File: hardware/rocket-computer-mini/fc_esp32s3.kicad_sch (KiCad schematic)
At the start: 35 parts, among them SW2 R-667995, U32 ESP32-S3RH2, U33 GD25Q128ESIG, Y3 ABS07-32.768KHZ-T, Y4 ECS-400-10-37B2-CKY-TR

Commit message: hardware: BOM re-use pass, DTC123J land fix, and pyro one-shot RC rework
Re-use pass across both rocket computers. The 17 new passives per board drawn
for the pack-fire/supercap rework carried no MPN field at all and would have
exported as blank BOM lines; assigning already-stocked parts rather than new
ones collapsed 15 would-be-new lines to zero.

Pyro arm one-shot (both boards):
- R131 added in parallel with R121 (2x 1M = 500k), C133/C138 moved to the
  stocked 22uF 0805, deleting the 10uF 0805 line.
- Not just BOM tidiness: SN74LVC1G17 Ii is +/-5uA max (SCES351Y Tbl 5-1). On
  the high-impedance timer node that offsets the asymptote to Vgate - Ii*R, so
  a single 1M settles near 1.0V, under VT+ max 1.92V, and a worst-case
  conforming part would NEVER trip the crowbar - the arm gate would stay up
  indefinitely. Max permissible R at the 2.83V supervisor floor is ~590k;
  500k clears it with ~19% headroom. Do not collapse R131 back into one 1M.
- R130 22k -> stocked 10k. With C133 now 22uF the reset stays at 0.22s, so the
  two edits cancel and the >=0.5s inter-arm spacing rule is unchanged.
- Ceiling ~3.4s nominal, 1.7s fast corner. The pyro sheet note now carries the
  leakage constraint so it cannot be "simplified" away later.

DTC123J land (affects Q3-Q6 on both boards, not only the rework):
- Widened to ROHM's own recommended pattern (Land Pattern Reference,
  Transistor, Rev.001 p.1/6): pair 0.6x0.7 on 1.0mm pitch, lone pad 0.7x0.7,
  rows 1.3 c-c. The inherited land was an imperial 14x30 mil pattern, 30-50%
  narrow across the lead with almost no side fillet on the widest terminal.
- Renamed DTC123JEBTL -> TRANS_SOT-416_EMT3-EMT3F_ROHM. ROHM publishes ONE
  land for both the gull-wing EMT3 and the flat-lead EMT3F, so naming it after
  either part number was misleading.
- rocket-computer-mini Q12 -> DTC123JETL, matching its Q3-Q6. MPN field only.

NOTE: the wider pads collide with existing routing on rocket-computer - two
genuine pad-to-via shorts (Q3 GND v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
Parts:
- D10: MPN XL-1005UGC -> NCD0402R1; Mfr Xinglight -> NationStar
- D11: MPN XL-1005UGC -> APHHS1005QBC/D; Mfr Xinglight -> Kingbright
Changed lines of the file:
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@@
 			)
 		)
-		(property "MPN" "XL-1005UGC"
+		(property "MPN" "NCD0402R1"
 			(at 254 104.14 0)
 			(hide yes)
@@
 			)
 		)
-		(property "Mfr" "Xinglight"
+		(property "Mfr" "NationStar"
 			(at 254 104.14 0)
 			(hide yes)
@@
 			)
 		)
-		(property "MPN" "XL-1005UGC"
+		(property "MPN" "APHHS1005QBC/D"
 			(at 268.605 104.14 0)
 			(hide yes)
@@
 			)
 		)
-		(property "Mfr" "Xinglight"
+		(property "Mfr" "Kingbright"
 			(at 268.605 104.14 0)
 			(hide yes)

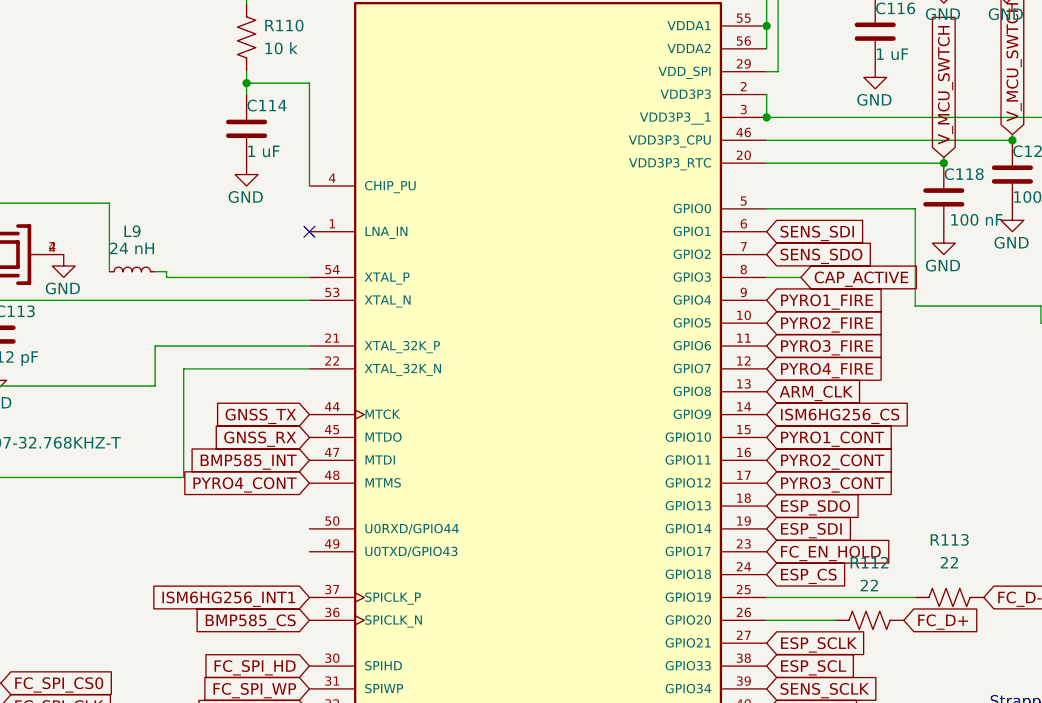
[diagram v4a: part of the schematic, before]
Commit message: rocket-computer-mini: supervised-MCU pyro arm (rework 3) replaces pump + one-shot (#981)
The 2026-08-26 charge-pump ARM carried a static rail->D12->D13 path that
parked the arm-FET gate at ~2.8 V with no clock (AON7534 Vth 1.4-2.2 V),
defeating the dead-man and phantom-tripping the one-shot after every boot
and disarm into a latched Q12 burn over its 150 mW rating. Rather than
patch it, the arm is rebuilt around liveness-by-supervision:

- ARM_GATE's only source is FC_ARM (FC GPIO44, static) via R132; R22 -> 100k
  bleed. FC reset/power-loss reverts the pin, so the node has no source.
- U46 TPS3813L30 window watchdog (WDT=VDD, WDR=GND: pet 94 ms - 2 s), petted
  on WDT_PET (GPIO8, ex-ARM_CLK); its open-drain RESET wire-ANDs into the
  FC's CHIP_PU RC and hard-resets a non-petting FC, which clears FC_ARM by
  construction. L30 variant is load-bearing: K33's VIT overlaps the
  2.86-2.94 V supercap hold-up floor.
- D16 Schottky = OC veto on the gate node (OC GPIO11, low = disarm); fire
  still needs the FC channel FETs, so a false fire takes two MCUs.

Deleted C131-C133, D12-D15, Q12, R121, R129-R131, U41 from schematic and
PCB (the cluster had no routed tracks; zones refilled, filled areas
unchanged). Netlist diff against the pre-edit baseline matches the spec
exactly; ERC 839->803 with no new classes; check_board_parity passes with
the mini's unplaced set now exactly the five new parts (U46, C139, R132,
R133, D16) awaiting placement. bom.csv regenerated and reconciled 0/0/0
(1 M and 74LVC1G17 lines drop, TPS3813 line added). Full rationale, fault
matrix, and bench list in arm-watchdog-rework.md. V10 not yet drawn.

Co-authored-by: Claude Fable 5 <noreply@anthropic.com>
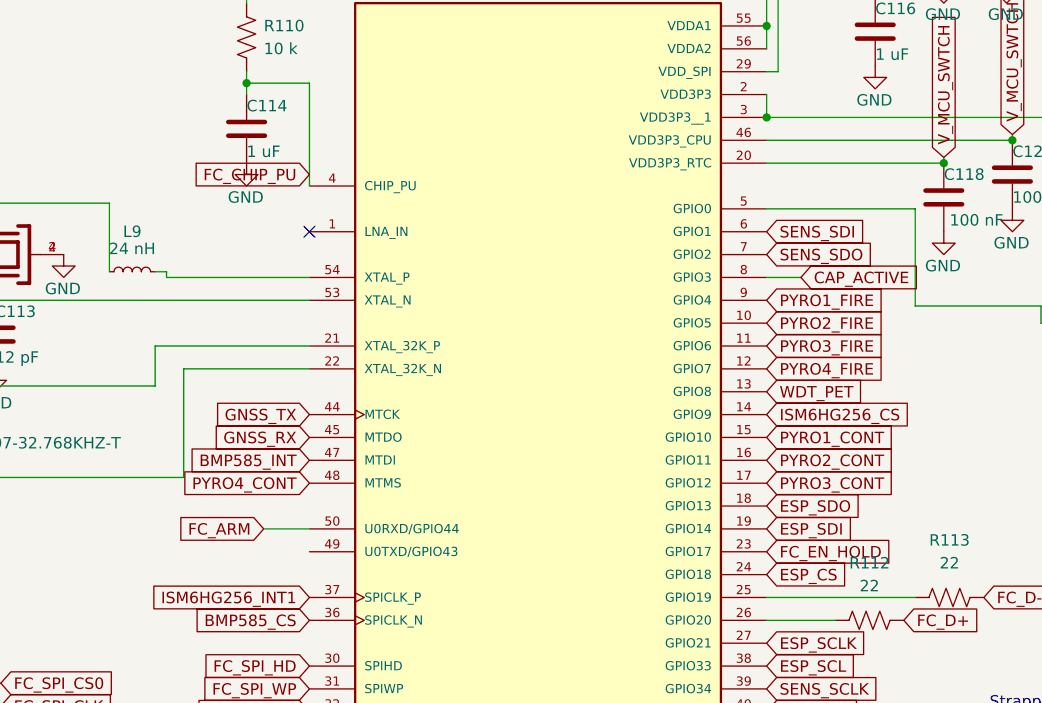
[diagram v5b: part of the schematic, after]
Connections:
- net FC_CHIP_PU: now reaches C114.1, R110.2, U32.4 (CHIP_PU)
- net FC_ARM: now reaches U32.50 (U0RXD/GPIO44)
- net ARM_CLK renamed WDT_PET
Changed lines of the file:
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@@
 		)
 	)
-	(global_label "ARM_CLK"
+	(global_label "WDT_PET"
 		(shape input)
 		(at 189.865 85.09 0)
@@
 			)
 		)
+	)
+	(wire
+		(pts
+			(xy 133.985 100.33) (xy 139.065 100.33)
+		)
+		(stroke
+			(width 0)
+			(type default)
+		)
+	)
+	(global_label "FC_ARM"
+		(shape input)
+		(at 133.985 100.33 180)
+		(fields_autoplaced yes)
+		(effects
+			(font
+				(size 1.27 1.27)
+			)
+			(justify right)
+		)
+		(property "Intersheetrefs" "${INTERSHEET_REFS}"
+			(at 133.985 100.33 0)
+			(hide yes)
+			(show_name no)
+			(do_not_autoplace no)
+			(effects
+				(font
+					(size 1.27 1.27)
+				)
+				(justify right)
+			)
+		)
+	)
+	(global_label "FC_CHIP_PU"
+		(shape input)
+		(at 139.065 60.96 180)
+		(fields_autoplaced yes)
+		(effects
+			(font
+				(size 1.27 1.27)
+			)
+			(justify right)
+		)
+		(property "Intersheetrefs" "${INTERSHEET_REFS}"
+			(at 139.065 60.96 0)
+			(hide yes)
+			(show_name no)
+			(do_not_autoplace no)
+			(effects
+				(font
+					(size 1.27 1.27)
+				)
+				(justify right)
+			)
+		)

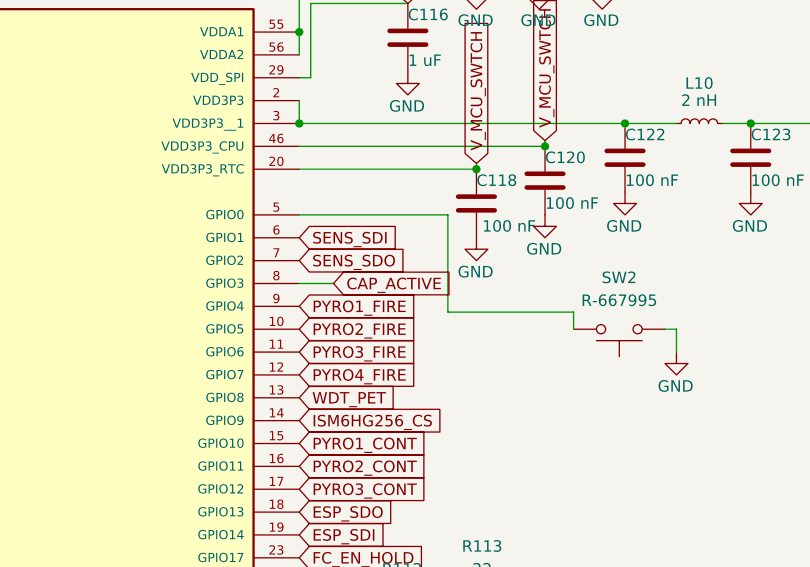
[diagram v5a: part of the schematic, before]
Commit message: hardware: TPS61094 supercap hold-up replaces the 4-IC chain on both computers (#983)
One TPS61094 (U47) now does the whole hold-up job on each board: bypass
V_BUCK -> +3V3 in normal operation, buck-charge the supercap at 100 mA to
a 2.5 V termination (VCHG bound: VIN - 800 mV), and boost from the cap to
a flat 3.3 V when V_BUCK collapses. The rail no longer sags through a
ride-through, so the 2.9 V cutoff chain and its analysis burden go away:
U40/U44 (LM66100), U42 (TPS22810), U45 (TPS3840), the 33 R charge
resistors (R120, V10 also R128), R127, CT caps C134/C136, and V_HOLD
decoupling C137/C138 are deleted; nets V_HOLD and V_UVLO_EN are gone.

New per board: U47 TPS61094DSSR, L11 2.2 uH (XGL4020-222ME, Isat 4.4 A;
the stocked VLS3012 line saturates at ~1.5 A and was rejected), R134/135/
136 = 4.75k/6.65k/22.1k 1% code resistors (OSEL 3.3 V, VCHG 2.5 V, ICHG
100 mA), C141/C142 10 uF, and a 100k/1M divider driving VBUCK_OK -- the
renamed CAP_ACTIVE, now INVERTED (HIGH = buck present; the TPS61094 has
no status pin, so the MCU pin watches V_BUCK directly).

Supercap: Eaton HV1020-2R7505-R (5 F, 2.7 V, 10x20 mm, ~40 mOhm) on both
boards, replacing the 5.5 V prismatics -- usable because the boost
decouples storage voltage from the rail. The V10 drops from two caps to
ONE (C139 deleted; ~2.6-3.9 s @0.7 A rides any firing event with margin;
the mini holds ~19 s @190 mA, ~4x today). New footprints: the XGL4020
land (Coilcraft doc 1529) and a horizontal D10 radial drawn to the house
no-courtyard-over-body convention; the V10 references the stock vertical
D10 P5 land (20 mm standing vs 28.5 today).

Verified on both boards: netlist diffs exactly to spec (only the intended
components and nets moved; final Eaton/VCHG pass changed exactly C130 and
R135 with zero net movement), ERC strictly better (mini 803->756, V10
1029->1012, including two pre-existing lib warnings that died with the
old parts), bom.csv regenerated and reconciled 0/0/0 -- repairing a
duplicate R22/R133 membe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
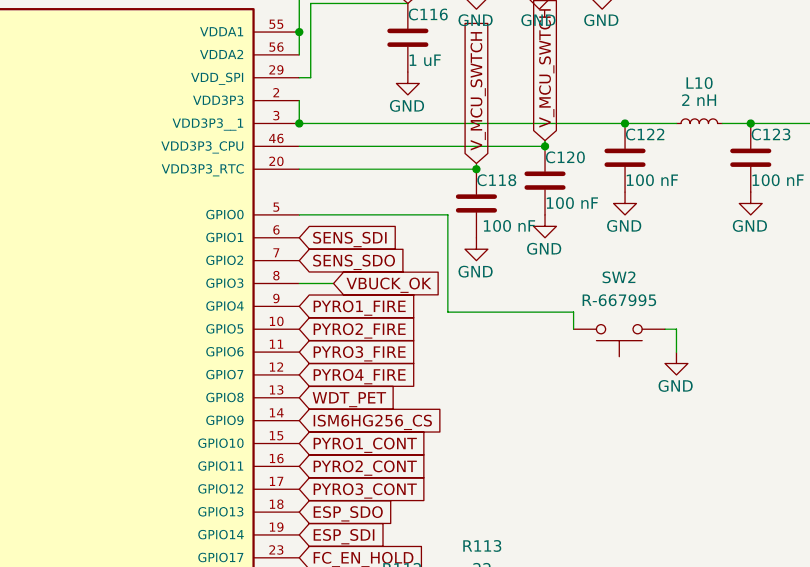
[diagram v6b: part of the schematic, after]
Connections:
- net CAP_ACTIVE renamed VBUCK_OK
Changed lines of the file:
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@@
 		)
 	)
-	(global_label "CAP_ACTIVE"
+	(global_label "VBUCK_OK"
 		(shape input)
 		(at 193.675 72.39 0)
